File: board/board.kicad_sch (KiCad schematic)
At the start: 21 parts, among them J1 001_I2C, J2 019_100BASE-T_with_CT, J3 019_100BASE-T_with_CT, J4 019_100BASE-T_with_CT, J5 019_100BASE-T_with_CT, J6 019_100BASE-T_with_CT

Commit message: added decoupling
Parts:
- added C20, C21, C22, C23, C24, C25, C26, C27, C28, C29: 100nF, Capacitor_SMD:C_0603_1608Metric, symbol Device:C_Small
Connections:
- net GND: now also C20.2, C21.2, C22.2, C23.2, C24.2, C25.2, C26.2, C27.2, C28.2, C29.2
- net at J6.7 (CT1): now also C20.1
- net at J6.8 (CT2): now also C25.1
- net at J4.7 (CT1): now also C21.1
- net at J4.8 (CT2): now also C26.1
- net at J2.7 (CT1): now also C24.1
- net at J2.8 (CT2): now also C29.1
- net at J5.7 (CT1): now also C22.1
- net at J5.8 (CT2): now also C27.1
- net at J3.7 (CT1): now also C23.1
- net at J3.8 (CT2): now also C28.1

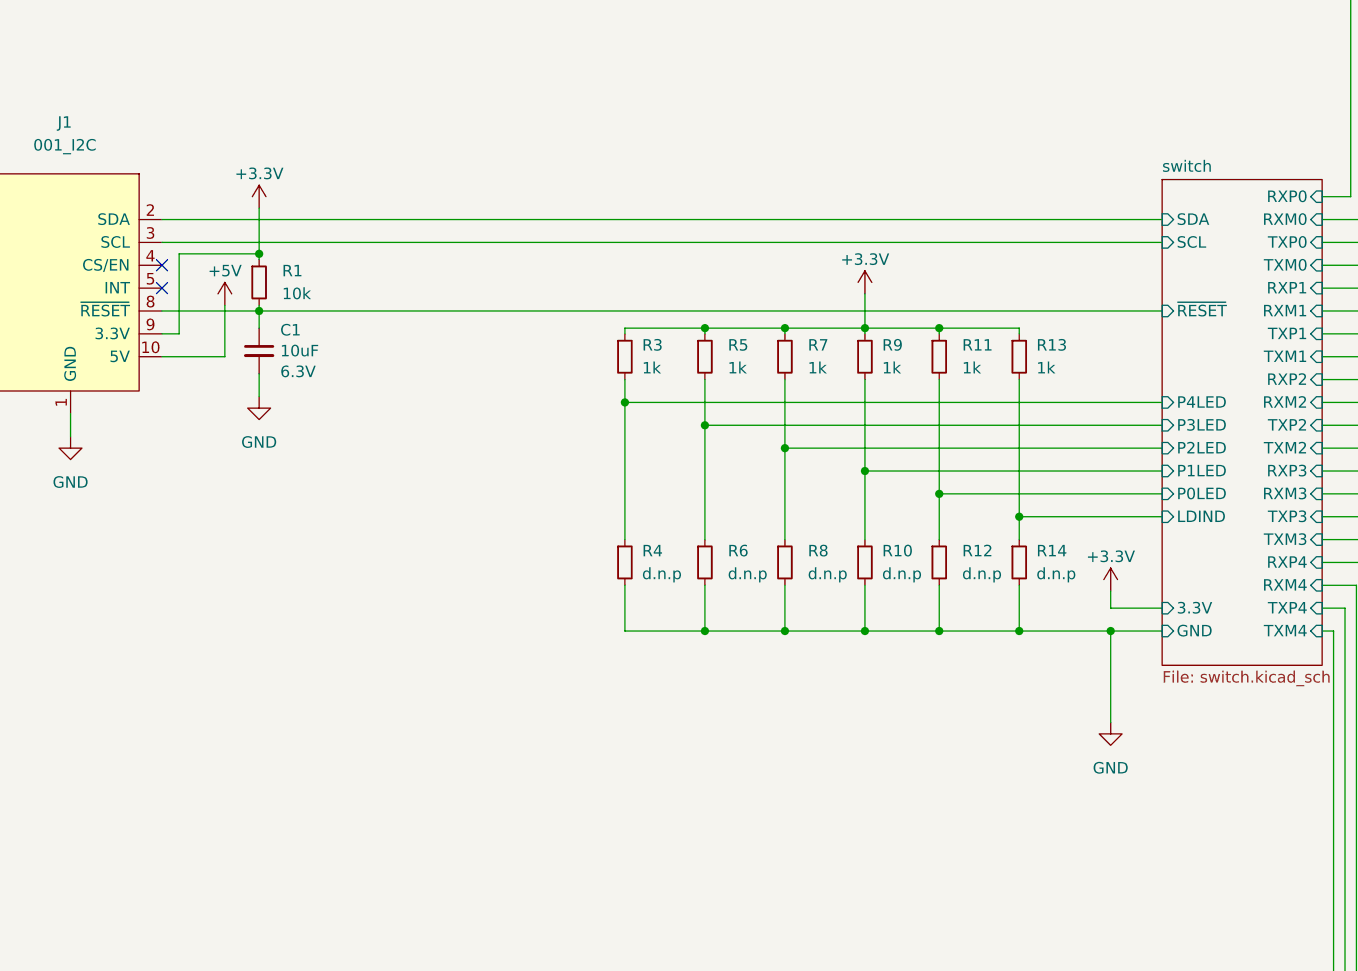
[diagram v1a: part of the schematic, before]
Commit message: added N filter for 3.3V input
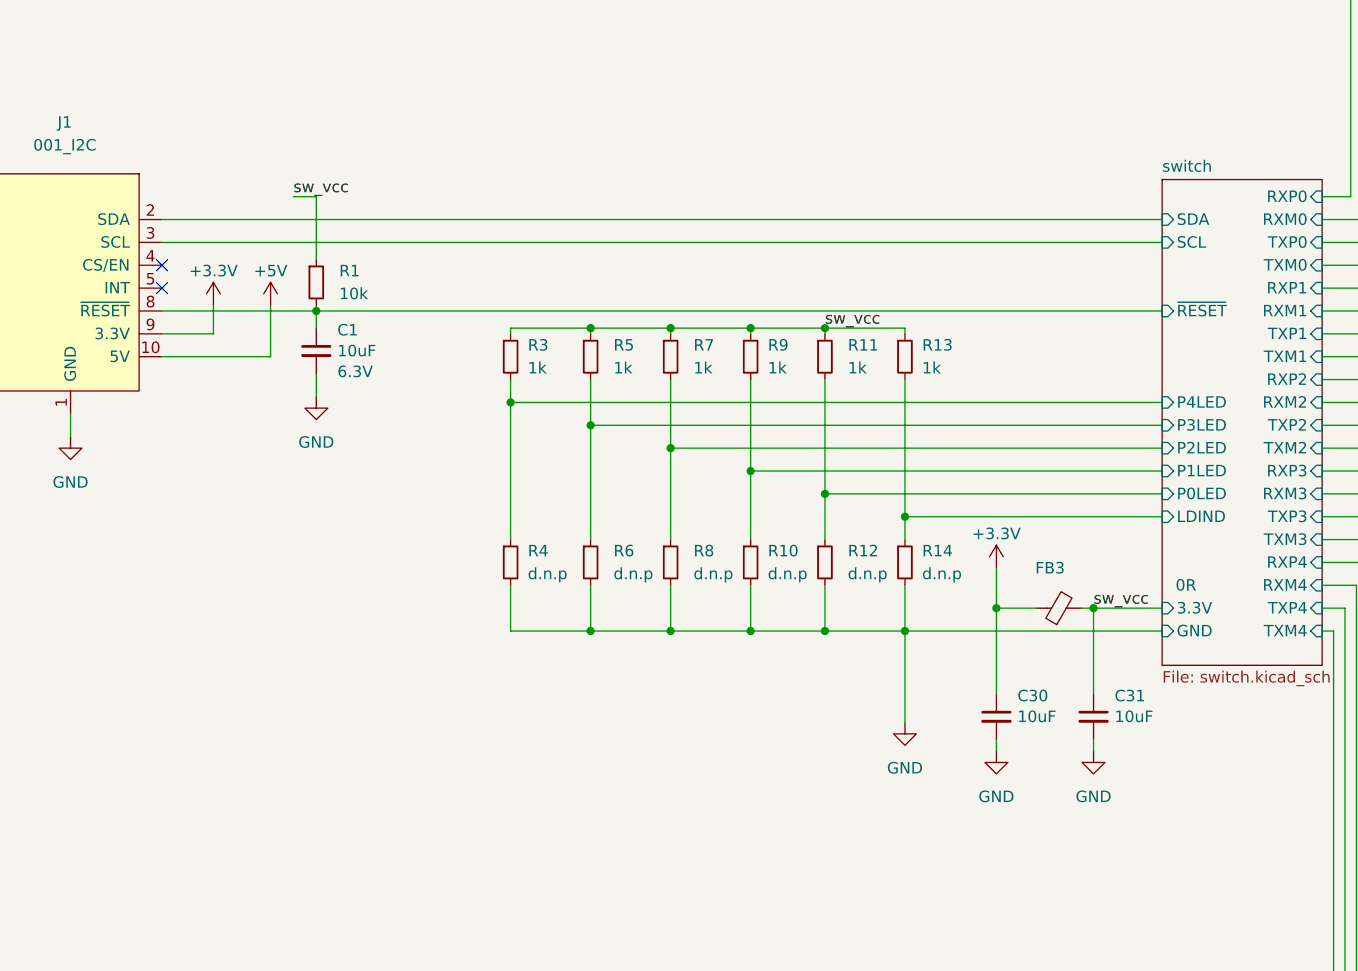
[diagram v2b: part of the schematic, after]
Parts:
- added C30, C31: 10uF, Capacitor_SMD:C_0603_1608Metric, symbol Device:C_Small
- added FB3: 0R, Inductor_SMD:L_0603_1608Metric, symbol Device:FerriteBead_Small
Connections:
- net +3.3V: now also C30.1, FB3.1; no longer R1.1, R11.1, R13.1, R3.1, R5.1, R7.1, R9.1
- net GND: now also C30.2, C31.2
- new net sw_vcc: C31.1, FB3.2, R1.1, R11.1, R13.1, R3.1, R5.1, R7.1, R9.1
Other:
- moved on the sheet: C1, R1, R10, R11, R12, R13, R14, R3, R4, R5, R6, R7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
